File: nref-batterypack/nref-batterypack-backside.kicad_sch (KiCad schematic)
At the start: 8 parts, among them J1 C1+, J2 C2-, J3 C3+, J4 C4-, J5 FRONT_CONN

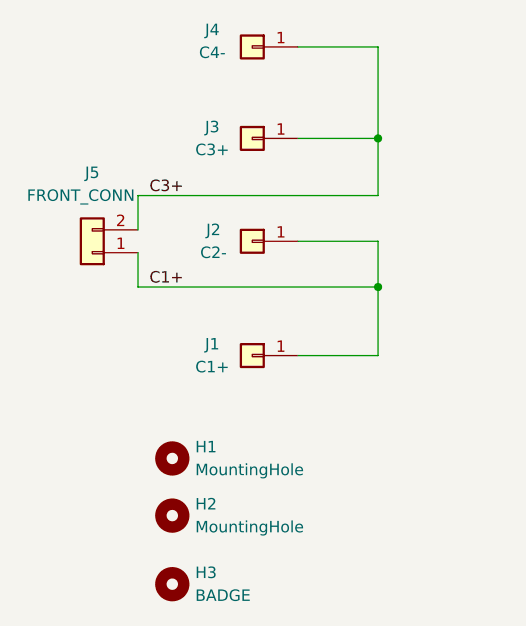
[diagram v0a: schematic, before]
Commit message: batterypack front/back: update board outline/mounting holes
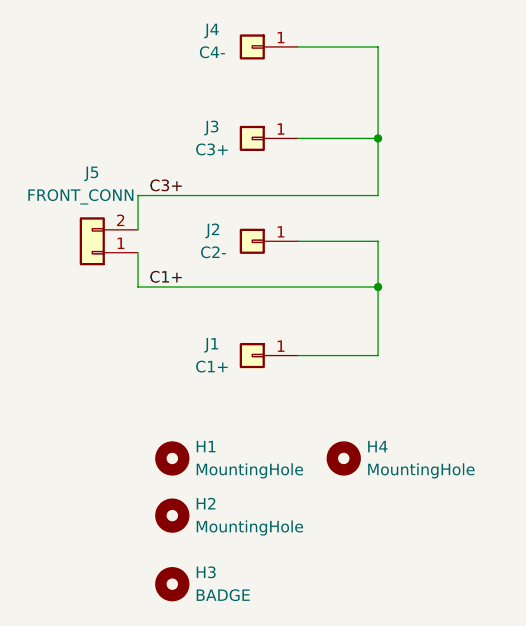
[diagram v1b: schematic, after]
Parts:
- added H4: MountingHole, MountingHole:MountingHole_2.2mm_M2, symbol Mechanical:MountingHole
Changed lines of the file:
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@@
+		)
+	)
+	(symbol
+		(lib_id "Mechanical:MountingHole")
+		(at 116.84 120.65 0)
+		(unit 1)
+		(exclude_from_sim yes)
+		(in_bom no)
+		(on_board yes)
+		(dnp no)
+		(fields_autoplaced yes)
+		(property "Reference" "H4"
+			(at 119.38 119.3799 0)
+			(effects
+				(font
+					(size 1.27 1.27)
+				)
+				(justify left)
+			)
+		)
+		(property "Value" "MountingHole"
+			(at 119.38 121.9199 0)
+			(effects
+				(font
+					(size 1.27 1.27)
+				)
+				(justify left)
+			)
+		)
+		(property "Footprint" "MountingHole:MountingHole_2.2mm_M2"
+			(at 116.84 120.65 0)
+			(effects
+				(font
+					(size 1.27 1.27)
+				)
+				(hide yes)
+			)
+		)
+		(property "Datasheet" "~"
+			(at 116.84 120.65 0)
+			(effects
+				(font
+					(size 1.27 1.27)
+				)
+				(hide yes)
+			)
+		)
+		(property "Description" "Mounting Hole without connection"
+			(at 116.84 120.65 0)
+			(effects
+				(font
+					(size 1.27 1.27)
+				)
+				(hide yes)
+			)
+		)
+		(instances
+			(project "nref-batterypack-backside"
+				(path "/992fdb00-2079-4fab-820a-500481d674d7"
+					(reference "H4")
+					(unit 1)
+				)
+			)
 		)
 	)
